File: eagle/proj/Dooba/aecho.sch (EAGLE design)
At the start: 47 parts, among them J3 SJ1-3523N, P1 I2C(SCL-SDA), P2 MP3_CTL(SCKR-SDI-DREQ-RST), P3 AMP_CTL(SHDN-CLK-UPDN), P4 PWR(GND-VIN-GND), P9 AOUT_L-GND-AOUT_R, U10 CS4334, U11 LM4811PDSO-10, U12 5.0V, U7 3.3V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

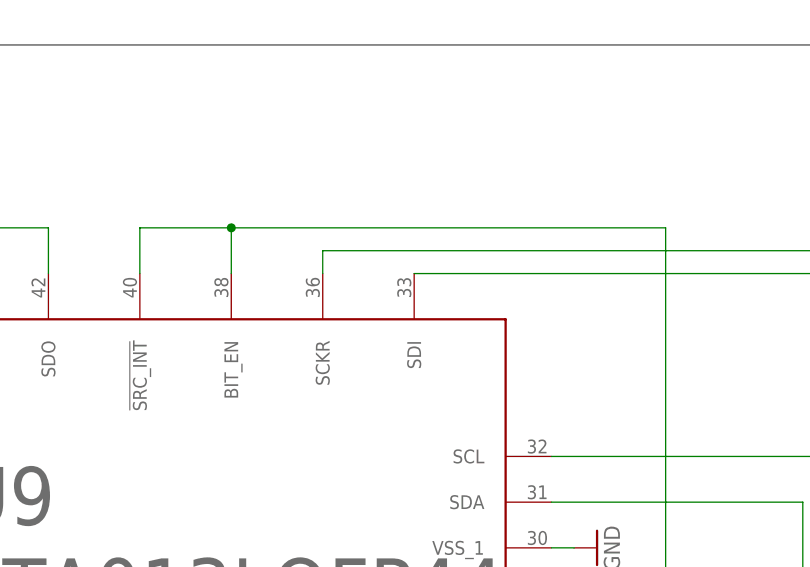
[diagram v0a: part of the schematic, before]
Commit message: Fixed STA013 Device in Eagle Library Fixed Aecho Board to use updated STA013 Fixed ioNode Schematic (74125 buffers for USB UART had their !OE tied to VCC...)
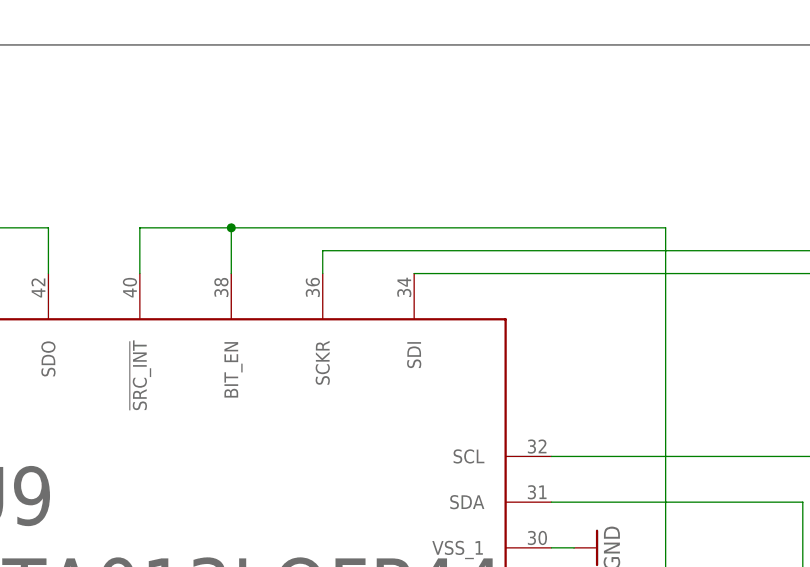
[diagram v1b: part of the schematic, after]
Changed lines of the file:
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@@
 <?xml version="1.0" encoding="utf-8"?>
 <!DOCTYPE eagle SYSTEM "eagle.dtd">
-<eagle version="7.7.0">
+<eagle version="7.3.0">
 <drawing>
 <settings>
